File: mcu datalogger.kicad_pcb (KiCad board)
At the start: 2 copper layers, 1 part

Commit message: Setup pcbnew
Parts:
- removed REF**: QFP80P900X900X120-32N, ATMEGA328P-AU:QFP80P900X900X120-32N
- added BT1: Battery, Connector_PinHeader_2.54mm:PinHeader_1x02_P2.54mm_Vertical, F.Cu at (129.3, 113.2)
- added C1: 0.1uF, Capacitor_SMD:C_0805_2012Metric, F.Cu at (151.7, 103.3)
- added C2: 22pF, Capacitor_SMD:C_0805_2012Metric, F.Cu at (151.7, 106.3)
- added C3: 22pf, Capacitor_SMD:C_0805_2012Metric, F.Cu at (151.7, 109.3)
- added C4: 0.1uF, Capacitor_SMD:C_0805_2012Metric, F.Cu at (151.7, 112.4)
- added C5: 100nF, Capacitor_SMD:C_0805_2012Metric, F.Cu at (151.7, 115.4)
- added D1: LED, LED_SMD:LED_0805_2012Metric, F.Cu at (156.1, 103.3)
- added D2: LED, LED_SMD:LED_0805_2012Metric, F.Cu at (156.1, 106.4)
- added H1: MountingHole, MountingHole:MountingHole_2.1mm, F.Cu at (129.9, 90.8)
- added H2: MountingHole, MountingHole:MountingHole_2.1mm, F.Cu at (129.9, 96.5)
- added H3: MountingHole, MountingHole:MountingHole_2.1mm, F.Cu at (129.9, 102.3)
- added H4: MountingHole, MountingHole:MountingHole_2.1mm, F.Cu at (129.9, 108.0)
- added J1: Conn_01x04_Pin, Connector_PinHeader_2.54mm:PinHeader_1x04_P2.54mm_Vertical, F.Cu at (167.2, 90.2)
- added J2: Conn_01x04_Pin, Connector_PinHeader_2.54mm:PinHeader_1x04_P2.54mm_Vertical, F.Cu at (171.8, 90.2)
- added J3: Conn_01x09_Pin, Connector_PinHeader_2.54mm:PinHeader_1x09_P2.54mm_Vertical, F.Cu at (162.6, 90.2)
- added J4: Conn_02x03_Odd_Even, Connector_PinHeader_2.54mm:PinHeader_2x03_P2.54mm_Vertical, F.Cu at (167.2, 102.4)
- added R1: 10K, Resistor_SMD:R_0805_2012Metric, F.Cu at (135.0, 89.4)
- added R2: 10k, Resistor_SMD:R_0805_2012Metric, F.Cu at (135.0, 92.3)
- added R3: 330, Resistor_SMD:R_0805_2012Metric, F.Cu at (135.0, 95.3)
- added R4: 10K, Resistor_SMD:R_0805_2012Metric, F.Cu at (135.0, 98.2)
- added R5: 330, Resistor_SMD:R_0805_2012Metric, F.Cu at (135.0, 101.2)
- added R6: 4.7K, Resistor_SMD:R_0805_2012Metric, F.Cu at (135.0, 104.1)
- added R7: 4.7K, Resistor_SMD:R_0805_2012Metric, F.Cu at (135.0, 107.1)
- added U1: 24LC1025, Package_SO:SOIC-8_5.3x5.3mm_P1.27mm, F.Cu at (142.4, 91.4)
- added U2: 24LC1025, Package_SO:SOIC-8_5.3x5.3mm_P1.27mm, F.Cu at (142.4, 98.4)
- added U3: DS1337S_, footprints:SOIC127P600X175-8N, F.Cu at (142.3, 116.5)
- added U4: ATMEGA328P-AU, footprints:QFP80P900X900X120-32N (2), F.Cu at (143.7, 107.5)
- added Y1: 32.768KHz, Crystal:Crystal_SMD_5032-2Pin_5.0x3.2mm_HandSoldering, F.Cu at (152.7, 90.5)
- added Y2: 16MHz, Crystal:Crystal_SMD_5032-2Pin_5.0x3.2mm_HandSoldering, F.Cu at (152.7, 95.8)

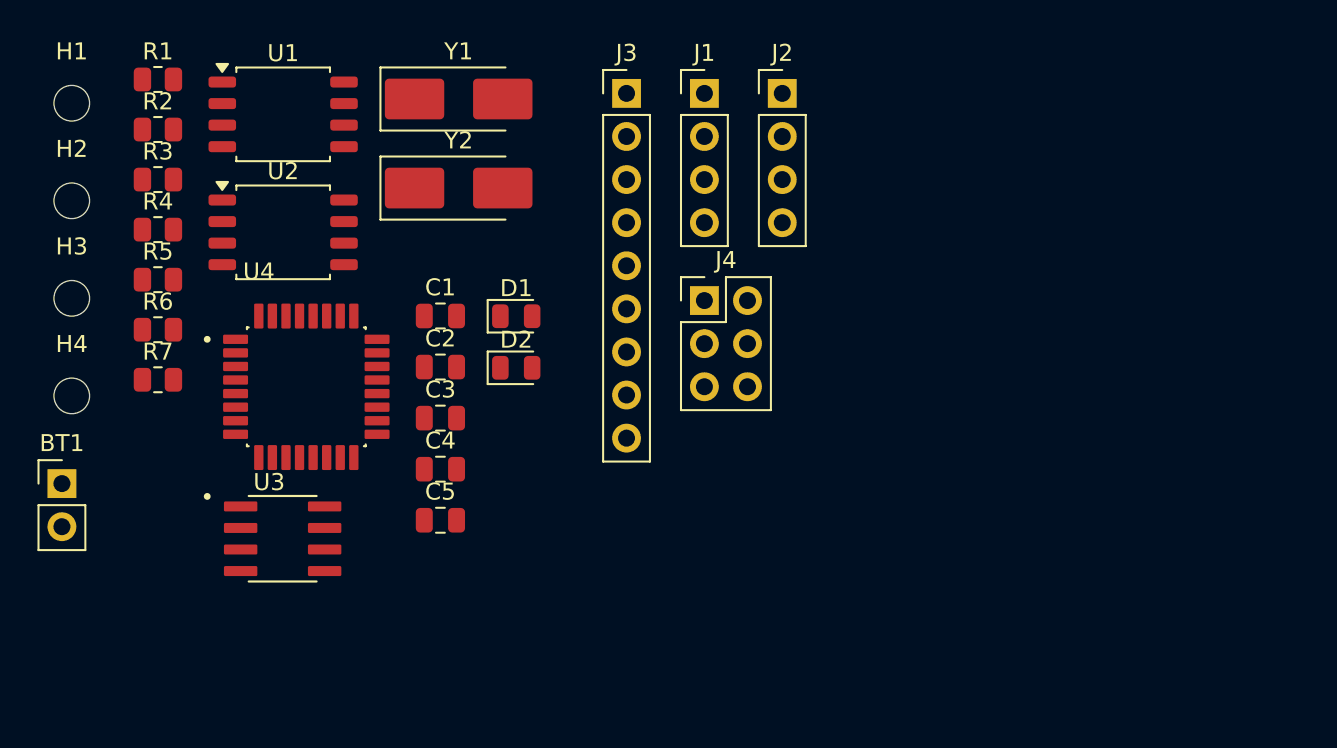
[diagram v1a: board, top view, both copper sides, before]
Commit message: Completed placement of footprints
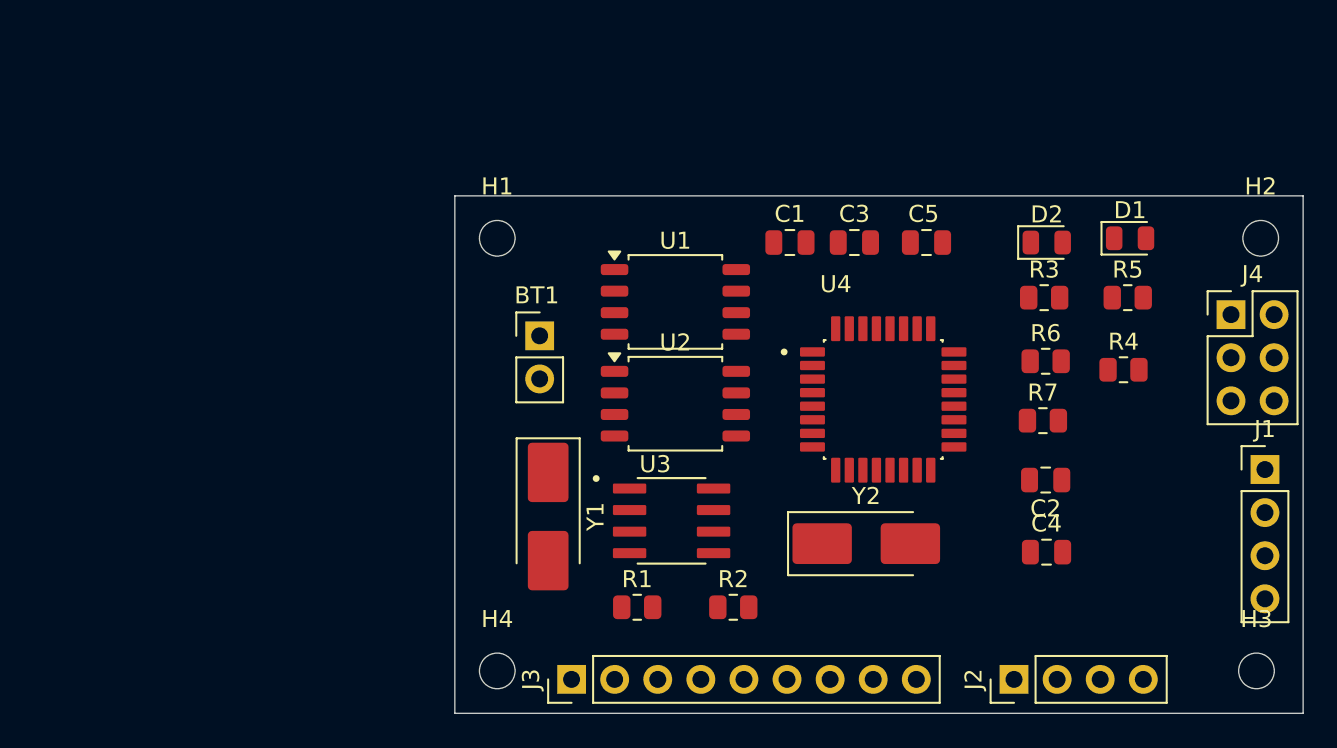
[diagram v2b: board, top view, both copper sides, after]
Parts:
- moved H3 73.2 mm to (199.8, 124.2)
- moved H2 70.1 mm to (200.0, 98.8)
- moved R4 57.5 mm to (191.9, 106.5)
- moved R5 57.2 mm to (192.2, 102.2)
- moved R3 52.7 mm to (187.2, 102.2)
- moved R6 52.4 mm to (187.3, 106.0)
- moved R7 52.2 mm to (187.2, 109.5)
- moved R2 44.1 mm to (168.9, 120.5)
- moved R1 42.0 mm to (163.2, 120.5)
- moved J1 39.8 mm to (200.2, 112.4)
- moved J2 37.1 mm to (185.5, 124.8), turned to 90 degrees
- moved D1 36.5 mm to (192.3, 98.8)
- moved C2 36.3 mm to (187.3, 113.0), turned to 180 degrees
- moved C4 36.1 mm to (187.4, 117.2)
- moved J3 34.7 mm to (159.4, 124.8), turned to 90 degrees
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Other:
- board outline added: 50 x 30.5 mm

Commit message: Routing sans GND and Vcc completed
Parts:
- moved U2 8.00 mm to (165.8, 100.5)
- moved U1 5.06 mm to (166.2, 107.5)
- moved R7 3.25 mm to (187.2, 106.2), turned to 180 degrees
- moved R6 3.25 mm to (187.2, 109.2), turned to 180 degrees
- moved R1 2.20 mm to (164.6, 118.8)
- moved Y1 2.02 mm to (160.0, 114.8)
- moved R2 1.77 mm to (168.7, 118.8)
- moved U3 1.73 mm to (166.8, 114.5)
- moved BT1 1.50 mm to (159.0, 104.5)
- moved C3 1.03 mm to (176.3, 100.0)
- moved C5 1.00 mm to (180.2, 100.0)
- moved C1 0.30 mm to (172.6, 99.0)
- turned Y2 to 180 degrees
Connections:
- U1 pad 5: unconnected-(U1-SDA-Pad5) -> /SDA
- U2 pad 5: unconnected-(U2-SDA-Pad5) -> /SDA
- U3 pad 5: unconnected-(U3-SDA-Pad5) -> /SDA
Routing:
- net /Vcc: track 0.00 -> 111.6 mm, vias 0 -> 1
- net /SCK: track 0.00 -> 110.9 mm, vias 0 -> 4
- net Net-(BT1-+): track 0.00 -> 67.1 mm, vias 0 -> 4
- net /SDA: track 0.00 -> 58.0 mm, vias 0 -> 2
- net GND: track 0.00 -> 45.1 mm, vias 0 -> 6
- net /TX: track 0.00 -> 39.0 mm, vias 0 -> 2
- net Net-(U4-PB7): track 0.00 -> 33.8 mm, vias 0 -> 2
- net /D2: track 0.00 -> 31.5 mm
- net /RX: track 0.00 -> 29.5 mm, vias 0 -> 2
- net /RESET: track 0.00 -> 29.2 mm, vias 0 -> 2
- net /MOSI: track 0.00 -> 28.6 mm
- net Net-(U4-PB6): track 0.00 -> 26.9 mm, vias 0 -> 2
- net /MISO: track 0.00 -> 26.4 mm, vias 0 -> 1
- net /D3: track 0.00 -> 26.3 mm, vias 0 -> 1
- net /D4: track 0.00 -> 25.3 mm, vias 0 -> 1
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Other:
- board size 50 x 30.5 mm -> 51 x 31.2 mm

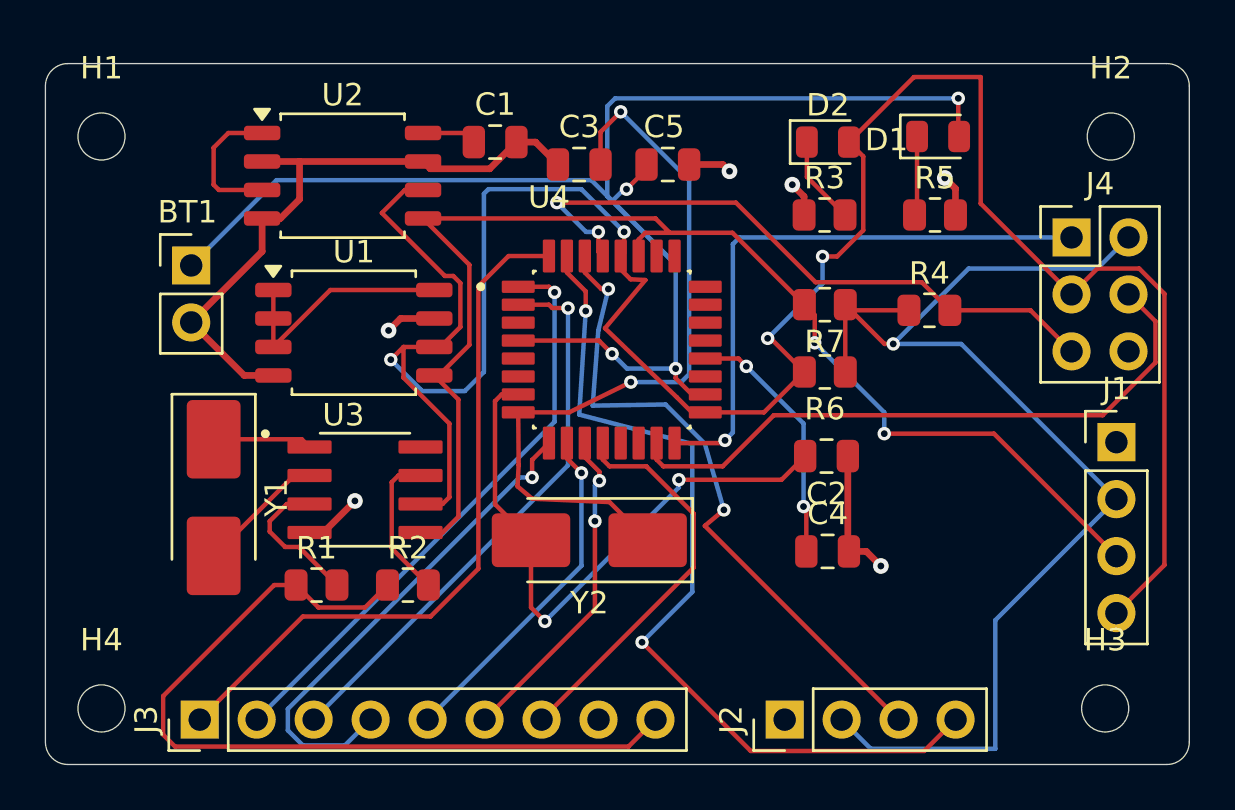
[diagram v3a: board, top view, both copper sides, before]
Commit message: Completed routing
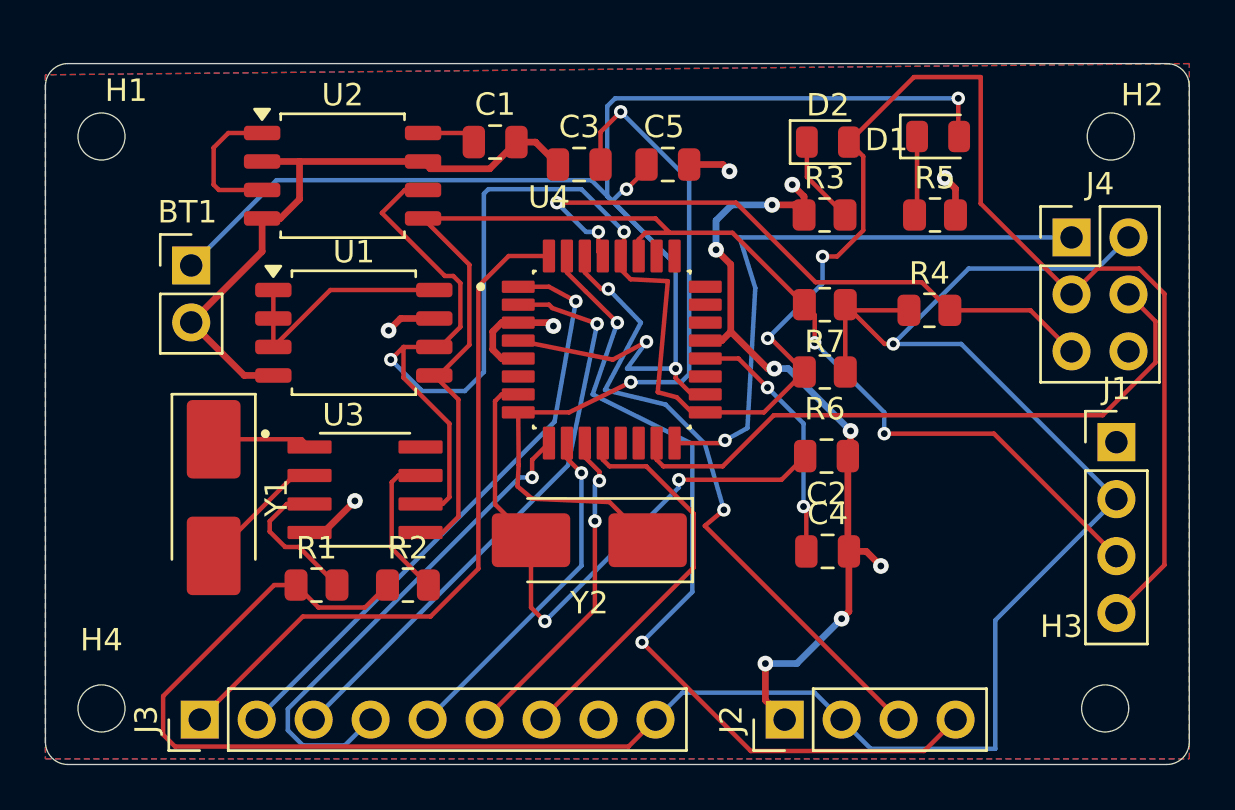
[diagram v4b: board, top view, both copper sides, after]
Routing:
- net GND: track 45.1 -> 79.7 mm, vias 6 -> 13
- net /Vcc: track 111.6 -> 120.9 mm
- net Net-(BT1-+): track 67.1 -> 69.2 mm
- net /D4: track 25.3 -> 26.2 mm
- net /D3: track 26.3 -> 27.0 mm
- added copper zone on F.Cu, net /Vcc
- added copper zone on B.Cu, net GND

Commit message: Fixed outstanding issues
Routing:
- net /RX: track 29.2 -> 30.8 mm
- net /MISO: track 26.9 -> 26.3 mm
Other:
- board text added: "2"
- board text added: "3"
- board text added: "4"
- board text added: "5"
- board text added: "6"
- board text added: "7"
- board text added: "8"
- board text added: "GND"
- board text added: "GPIO"
- board text added: "I2C"
- board text added: "ICSP"
- board text added: "ICSP MISO | VCC SCK | MOSI RESET| GND"
- board text added: "RX"
- board text added: "SCK"
- board text added: "SDA"
- board text added: "SERIAL"
- board text added: "TX"
- board text added: "VCC"
